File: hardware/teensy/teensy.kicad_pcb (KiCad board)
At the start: 2 copper layers, 127 x 76.2 mm, 81 parts, among them U1 Teensy3.5

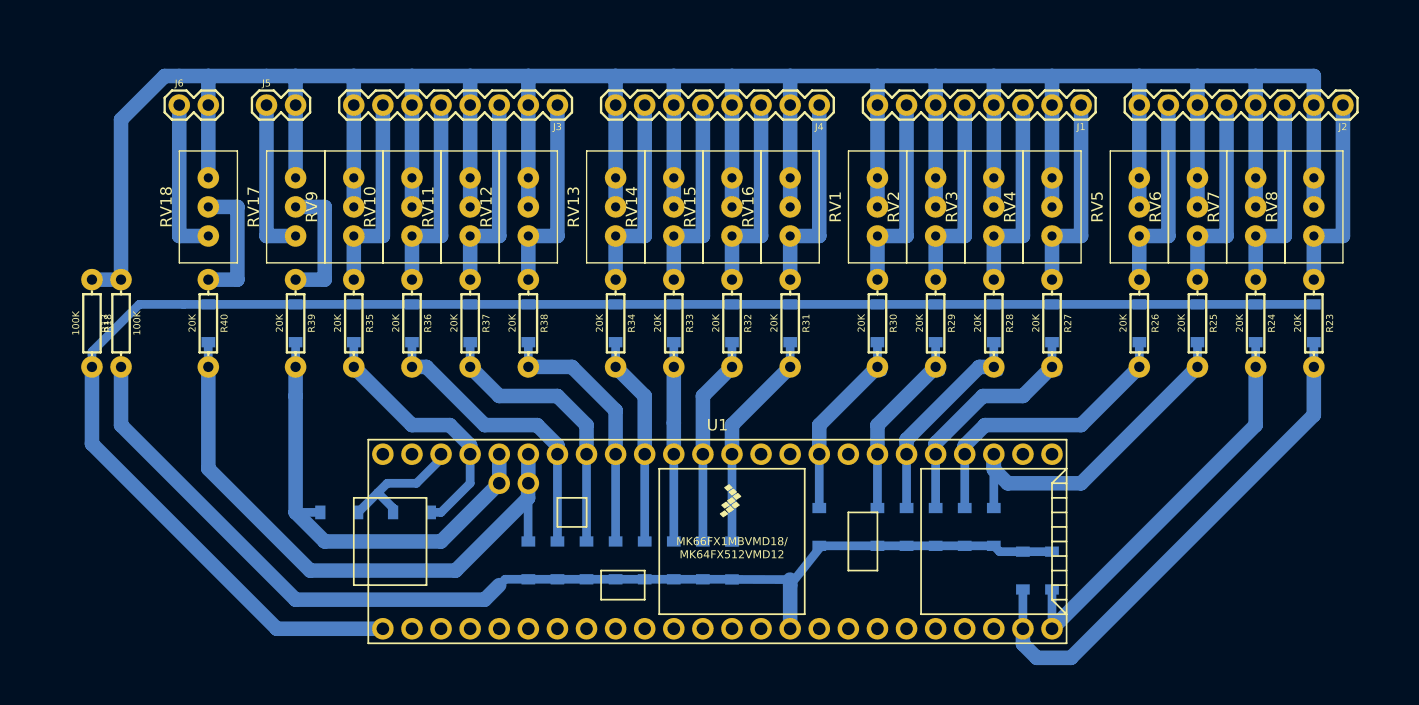
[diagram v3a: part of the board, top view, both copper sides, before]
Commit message: moved a few traces
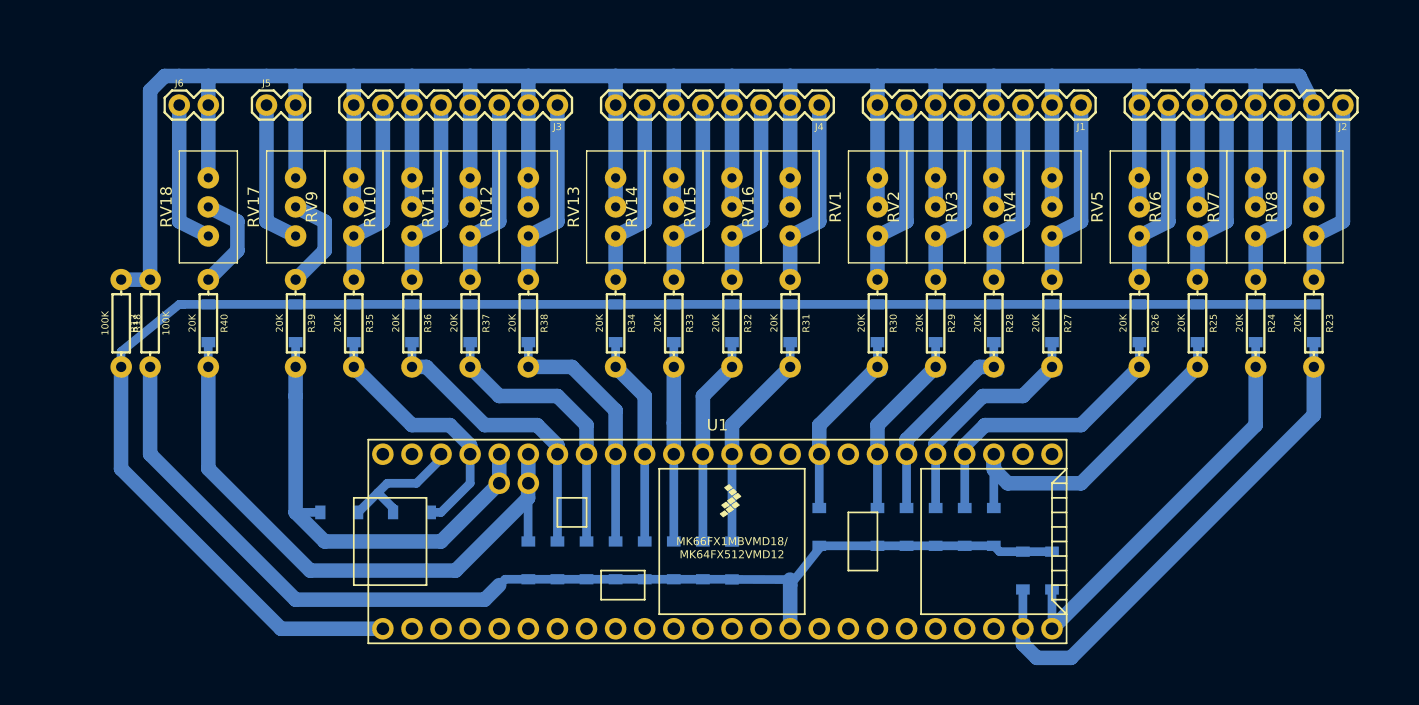
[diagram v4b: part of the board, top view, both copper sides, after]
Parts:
- moved R18 2.55 mm to (101.6, 118.1)
- moved R17 2.54 mm to (104.1, 118.1)
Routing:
- net /GND: track 148.5 -> 144.5 mm
- net /L1_SCALED: track 11.4 -> 8.97 mm
- net /L2_SCALED: track 11.4 -> 8.97 mm
- net /CT_BIAS: track 322.9 -> 320.9 mm
- net /3.3V: track 99.5 -> 98.5 mm
- net /ct16: track 17.8 -> 16.8 mm
- net /L2: track 14.0 -> 13.0 mm
- net /L1: track 14.0 -> 13.0 mm
- net /ct9: track 17.8 -> 16.8 mm
- net /ct8: track 17.8 -> 16.8 mm
- net /ct7: track 17.8 -> 16.8 mm
- net /ct6: track 17.8 -> 16.8 mm
- net /ct5: track 17.8 -> 16.8 mm
- net /ct4: track 17.8 -> 16.8 mm
- net /ct3: track 17.8 -> 16.8 mm
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
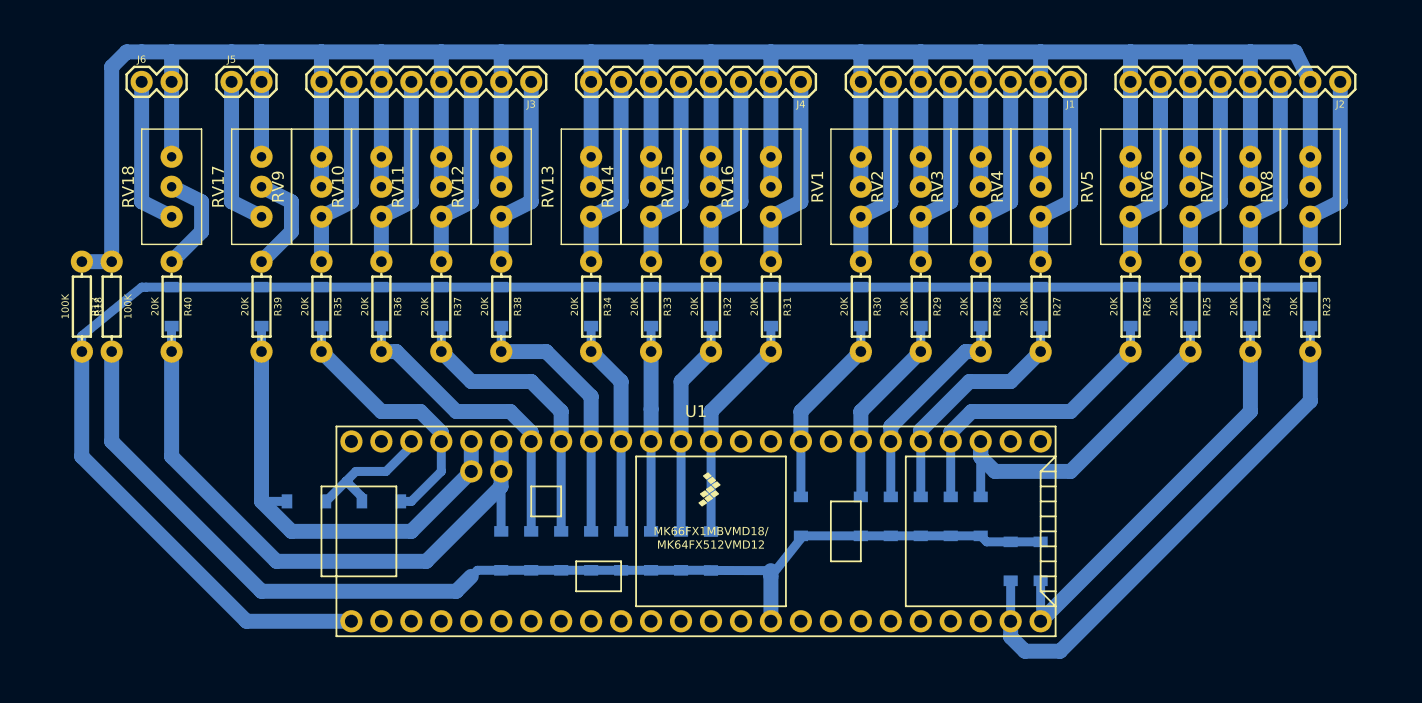
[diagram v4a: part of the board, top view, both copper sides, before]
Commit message: accommodate actual 27 mil bit
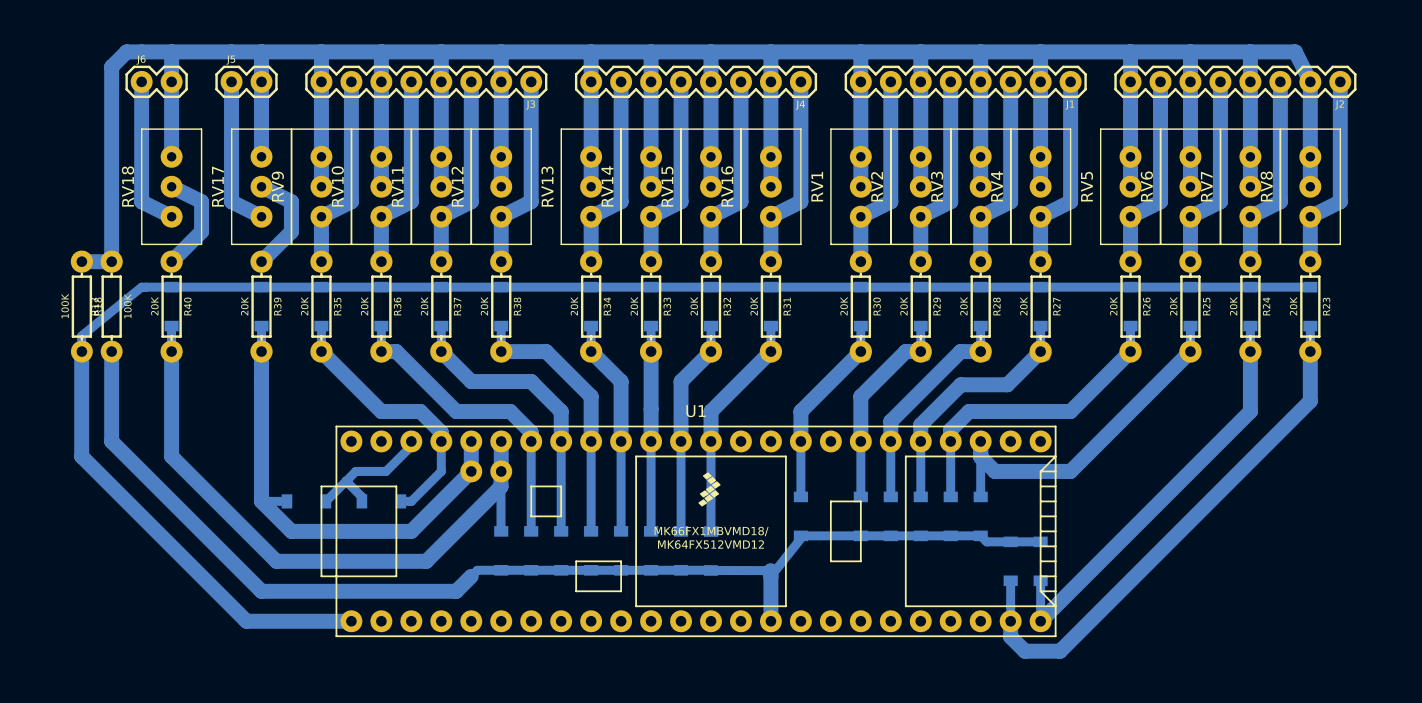
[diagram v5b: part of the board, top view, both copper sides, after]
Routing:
- net /A20: track 17.2 -> 18.0 mm

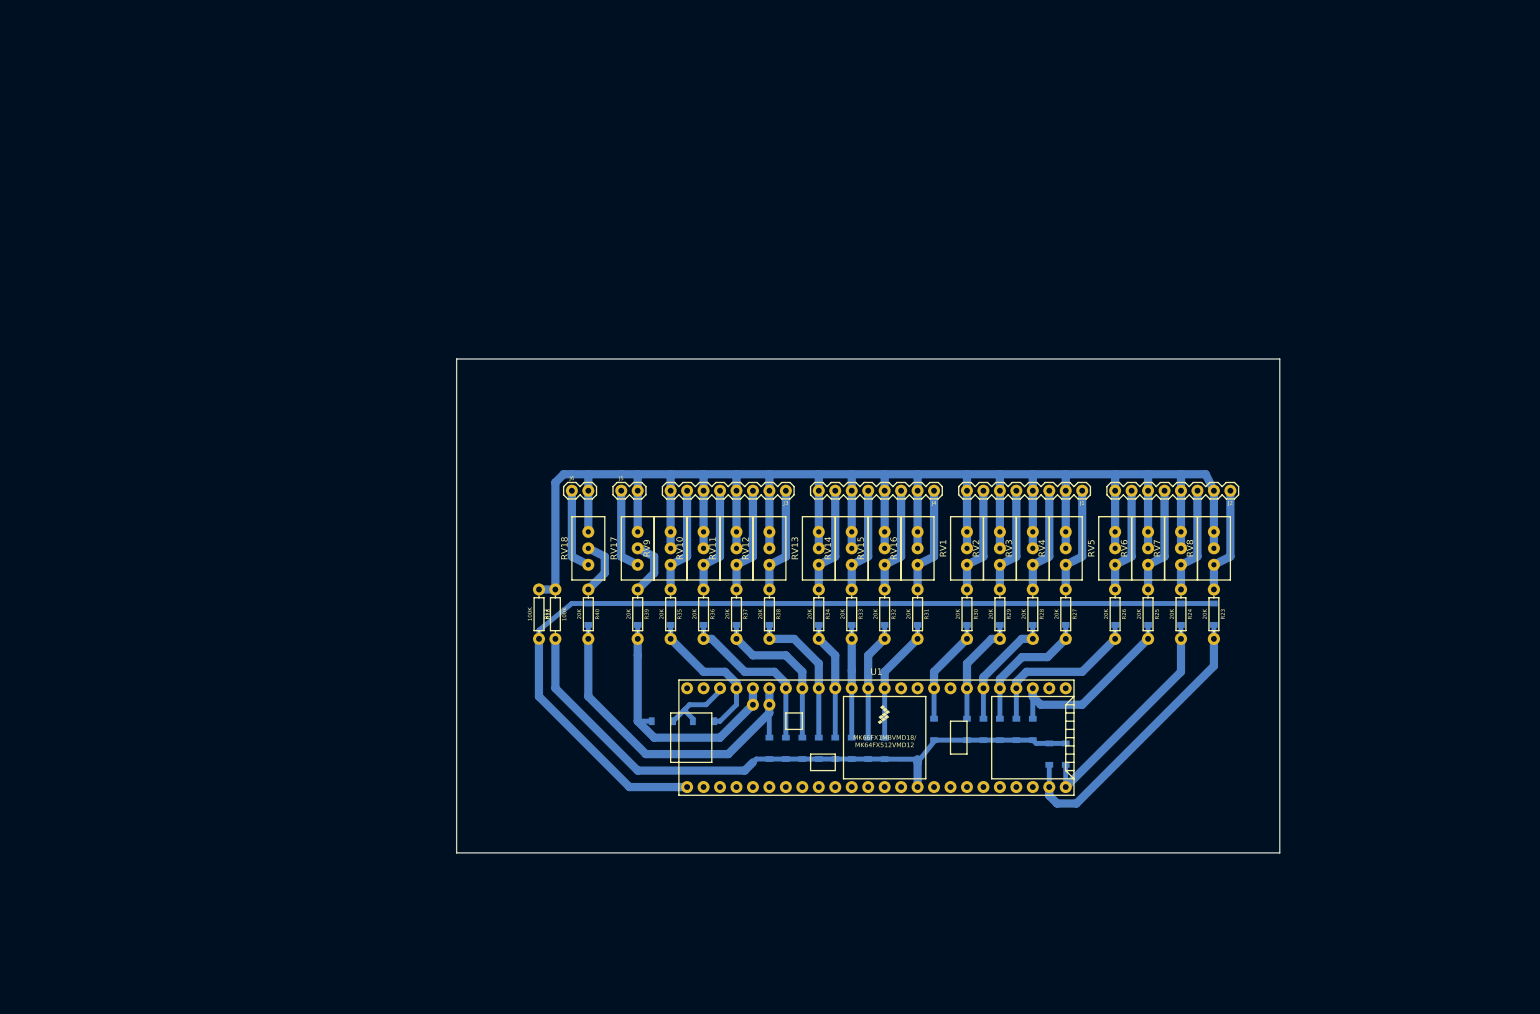
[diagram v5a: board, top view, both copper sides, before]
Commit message: formatting for printing
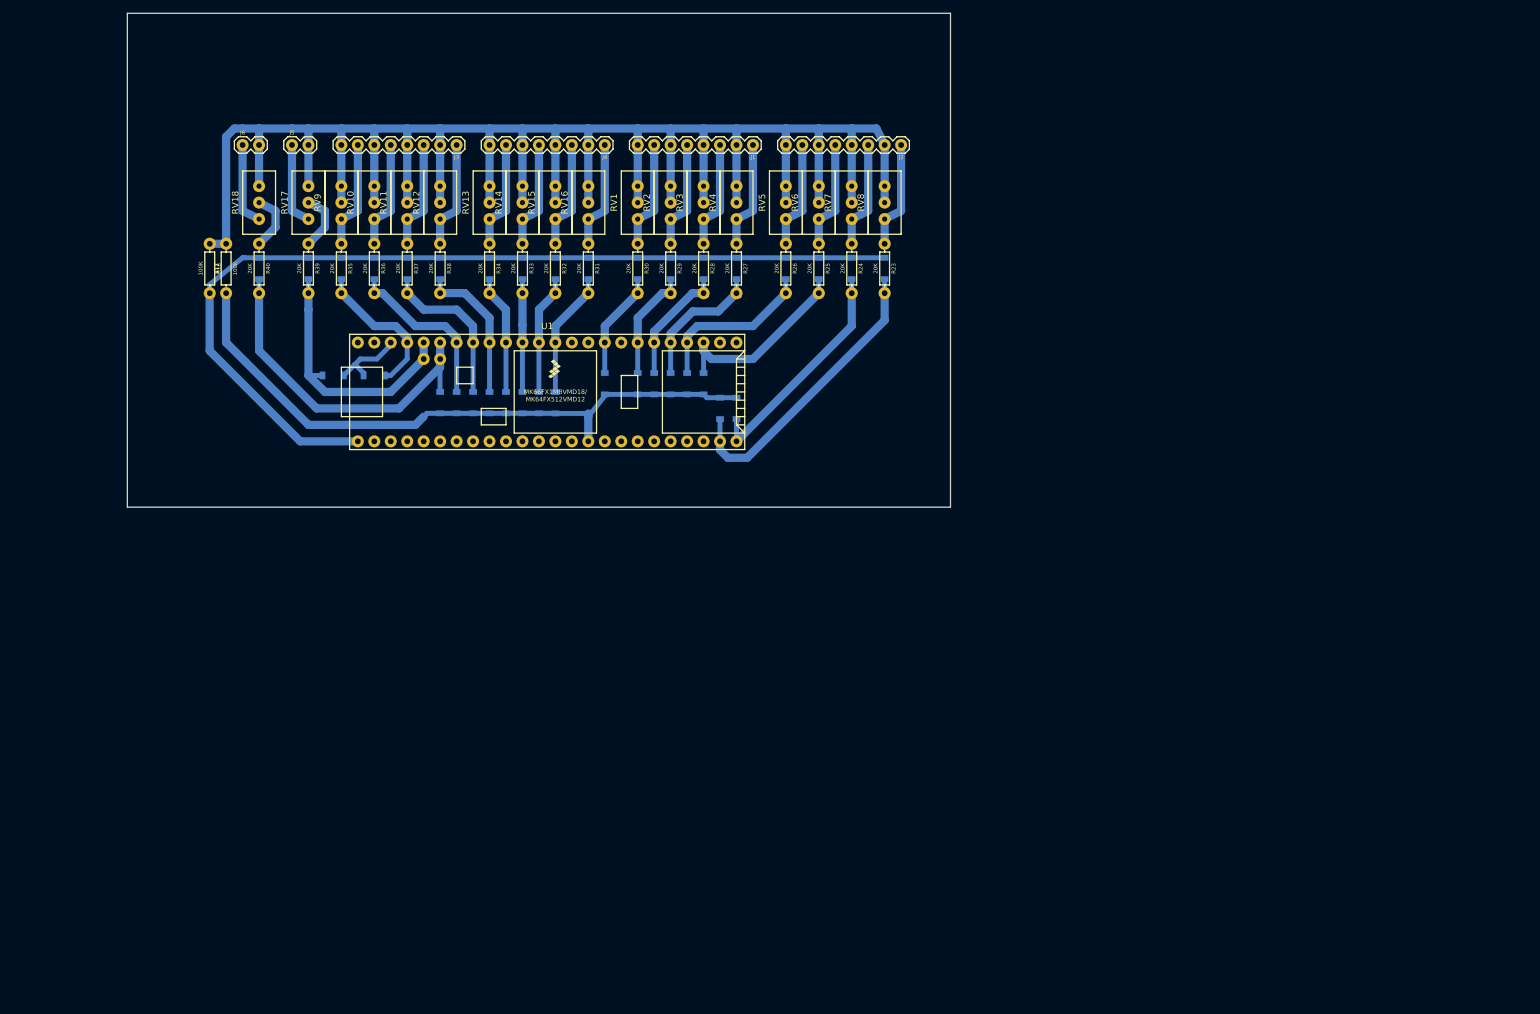
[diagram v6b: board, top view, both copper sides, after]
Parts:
- moved D1 73.7 mm to (154.9, 64.8)
- moved D11 73.7 mm to (127.0, 64.8)
- moved D17 73.7 mm to (109.2, 64.8)
- moved D21 73.7 mm to (99.1, 64.8)
- moved D29 73.7 mm to (81.3, 64.8)
- moved D34 73.7 mm to (69.8, 81.3)
- moved D5 73.7 mm to (144.8, 64.8)
- moved D7 73.7 mm to (139.7, 64.8)
- moved J2 73.7 mm to (157.5, 45.7)
- moved J6 73.7 mm to (55.9, 45.7)
- moved R18 73.7 mm to (50.8, 64.8)
- moved R23 73.7 mm to (154.9, 64.8)
- moved R25 73.7 mm to (144.8, 64.8)
- moved R26 73.7 mm to (139.7, 64.8)
- moved R28 73.7 mm to (127.0, 64.8)
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
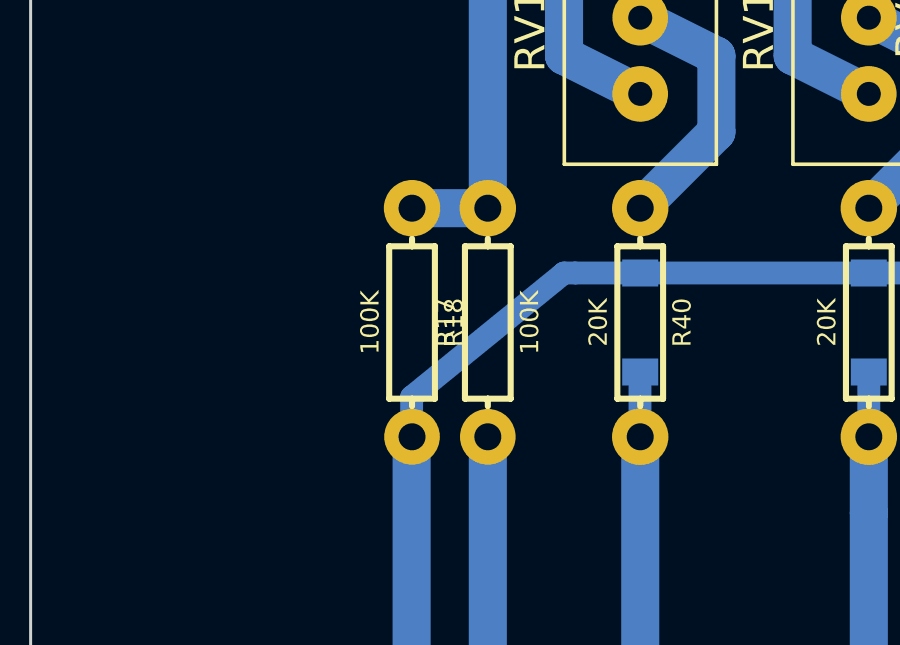
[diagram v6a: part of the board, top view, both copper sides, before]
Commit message: add capacitor for bias smoothing
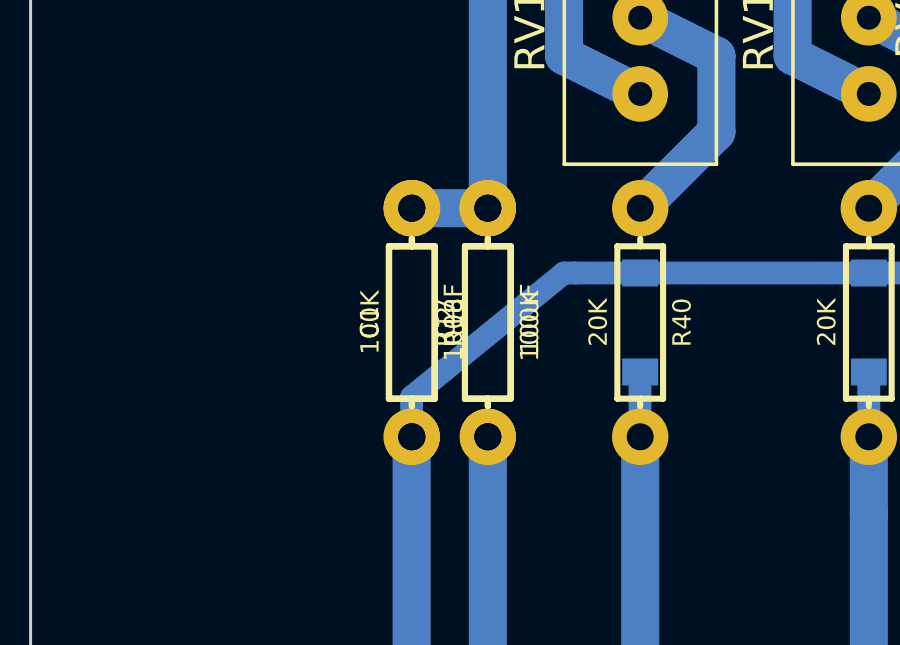
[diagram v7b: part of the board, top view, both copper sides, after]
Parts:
- added C1: 100uF, Resistors:AXIAL-0.3, F.Cu at (50.8, 64.8)
- added C2: 100uF, Resistors:AXIAL-0.3, F.Cu at (53.3, 64.8)
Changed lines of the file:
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@@
     (drawings 4)
     (tracks 285)
-    (modules 81)
+    (modules 83)
     (nets 70)
   )
@@
   (net 68 "Net-(U1-Pad52)")
   (net 69 "Net-(U1-Pad53)")
+  (module "Resistors:AXIAL-0.3" (layer "F.Cu")
+    (at 53.34 64.77 90)
+    (descr "AXIAL-0.3")
+    (tags "AXIAL-0.3")
+    (attr virtual)
+    (fp_text reference "C2" (at 0 -1.397 90) (layer "F.SilkS")
+      (effects (font (size 0.6096 0.6096) (thickness 0.127)))
+    )
+    (fp_text value "100uF" (at 0 1.397 90) (layer "F.SilkS")
+      (effects (font (size 0.6096 0.6096) (thickness 0.127)))
+    )
+    (fp_line (start -2.54 0) (end -2.794 0) (layer "F.SilkS") (width 0.2032))
+    (fp_line (start 2.54 0) (end 2.794 0) (layer "F.SilkS") (width 0.2032))
+    (fp_line (start -2.54 0) (end -2.54 -0.762) (layer "F.SilkS") (width 0.2032))
+    (fp_line (start -2.54 0.762) (end -2.54 0) (layer "F.SilkS") (width 0.2032))
+    (fp_line (start 2.54 0.762) (end -2.54 0.762) (layer "F.SilkS") (width 0.2032))
+    (fp_line (start 2.54 0) (end 2.54 0.762) (layer "F.SilkS") (width 0.2032))
+    (fp_line (start 2.54 -0.762) (end 2.54 0) (layer "F.SilkS") (width 0.2032))
+    (fp_line (start -2.54 -0.762) (end 2.54 -0.762) (layer "F.SilkS") (width 0.2032))
+    (pad "P$2" thru_hole circle (at 3.81 0 90) (size 1.8796 1.8796) (drill 0.89916) (layers *.Cu *.Mask)
+      (solder_mask_margin 0.1016))
+    (pad "P$1" thru_hole circle (at -3.81 0 90) (size 1.8796 1.8796) (drill 0.89916) (layers *.Cu *.Mask)
+      (solder_mask_margin 0.1016))
+  )
+  (module "Resistors:AXIAL-0.3" (layer "F.Cu")
+    (at 50.8 64.77 90)
+    (descr "AXIAL-0.3")
+    (tags "AXIAL-0.3")
+    (attr virtual)
+    (fp_text reference "C1" (at 0 -1.397 90) (layer "F.SilkS")
+      (effects (font (size 0.6096 0.6096) (thickness 0.127)))
+    )
+    (fp_text value "100uF" (at 0 1.397 90) (layer "F.SilkS")
+      (effects (font (size 0.6096 0.6096) (thickness 0.127)))
+    )
+    (fp_line (start -2.54 0) (end -2.794 0) (layer "F.SilkS") (width 0.2032))
+    (fp_line (start 2.54 0) (end 2.794 0) (layer "F.SilkS") (width 0.2032))
+    (fp_line (start -2.54 0) (end -2.54 -0.762) (layer "F.SilkS") (width 0.2032))
+    (fp_line (start -2.54 0.762) (end -2.54 0) (layer "F.SilkS") (width 0.2032))
+    (fp_line (start 2.54 0.762) (end -2.54 0.762) (layer "F.SilkS") (width 0.2032))
+    (fp_line (start 2.54 0) (end 2.54 0.762) (layer "F.SilkS") (width 0.2032))
+    (fp_line (start 2.54 -0.762) (end 2.54 0) (layer "F.SilkS") (width 0.2032))
+    (fp_line (start -2.54 -0.762) (end 2.54 -0.762) (layer "F.SilkS") (width 0.2032))
+    (pad "P$2" thru_hole circle (at 3.81 0 90) (size 1.8796 1.8796) (drill 0.89916) (layers *.Cu *.Mask)
+      (solder_mask_margin 0.1016))
+    (pad "P$1" thru_hole circle (at -3.81 0 90) (size 1.8796 1.8796) (drill 0.89916) (layers *.Cu *.Mask)
+      (solder_mask_margin 0.1016))
+  )
   (module "teensy:Teensy35_36_EMON" (layer "F.Cu")
     (at 102.87 83.82)

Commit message: fix the kicad, also tuning
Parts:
- removed R17, R18: 100K, Resistors:AXIAL-0.3
- added U2: 200K, Potentiometer_THT:Potentiometer_Bourns_3296W_Vertical, F.Cu at (41.9, 68.6)
- C1, C2: footprint Resistors:AXIAL-0.3 -> Capacitors:CPOL-RADIAL-5MM-10MM
- moved C2 30.3 mm to (27.9, 81.3), turned to -90 degrees
- moved C1 27.9 mm to (26.7, 50.8), turned to -90 degrees
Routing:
- net /CT_BIAS: track 320.9 -> 300.0 mm
- net /GND: track 144.5 -> 127.7 mm
